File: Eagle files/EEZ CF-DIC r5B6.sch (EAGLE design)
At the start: 260 parts, among them IC1 VIPer35L, IC2 SI8233BB-D-IS1, IC3 LM5041B, IC4 LM258D, IC5 IR11688STRPBF, IC6 LM258D, IC7 TL103W, P1 T910W-50K, Q1 MMBT5551, Q2 C3M0280090D, Q3 C3M0280090D, Q4 NYC0102BLT1G, Q5 C3M0280090D, Q6 C3M0280090D, Q7 FDD86250-F085, Q8 FDD86250-F085, X1 39-30-3035, X2 22-05-7085, X3 B2B-ZR, X4 39-30-1020

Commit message: r5B6 version
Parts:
- added C80: N.C., rcl:C-EUC0805
- added D28: BAS316, EEZ_Lib1:DIODESOD323R
- added L9: IHLP2020CZER3R3M11, EEZ_inductors_and_transformers:IHLP-2020BZ-11
- added Q10, Q9: BC856C, transistor:BC857C-PNP-SOT23-BEC
- added R90: 5K6, rcl:R-EU_R0805
- added R91: 7K5, rcl:R-EU_R0805
- added R92: 220R, rcl:R-EU_R0805
- added R93, R94: 10K, rcl:R-EU_R0805
- added R95: 150K, rcl:R-EU_R0805
- added R96: 39K, rcl:R-EU_R0805
- added R97: 15K, rcl:R-EU_R0805
- added R98: 51K, rcl:R-EU_R0805
- added SH4: (no value), EEZ_Lib1:SHORTNOHOLE
- C1: value MKP-X2-220NR15/310 -> 3n3; device rcl:C-EU150-072X183 -> rcl:C-EUC0805
- C10: value EEEFK1V470P -> 1u; device EEZ_Lib1:ECAPPANASONIC_H -> rcl:C-EUC0805
- C11: value 1u -> EEEFK1V470P; device rcl:C-EUC0805 -> EEZ_Lib1:ECAPPANASONIC_H
- C12: value 1n/1kV -> EEEFK1V470P; device rcl:C-EUC1210 -> EEZ_Lib1:ECAPPANASONIC_H
- C13: value UCY2G6R8MPD -> 1u; device EEZ_Lib1:ECAP5G_10.5MM -> rcl:C-EUC0805
- C14: value EEEFK1V470P -> 1n/1kV; device EEZ_Lib1:ECAPPANASONIC_H -> rcl:C-EUC1210
- C15, C22: value 4u7 -> 3n3; device rcl:C-EUC1206 -> rcl:C-EUC0805
- C16: value 3n3 -> UCY2G6R8MPD; device rcl:C-EUC0805 -> EEZ_Lib1:ECAP5G_10.5MM
- C17: value CY1Y-4N7 -> 3n3; device EEZ_Lib1:C-EUCY -> rcl:C-EUC0805
- C18: value 100n -> EEEFK1V470P; device rcl:C-EUC0603 -> EEZ_Lib1:ECAPPANASONIC_H
- C19: value 3n3 -> 4u7; device rcl:C-EUC0805 -> rcl:C-EUC1206
- C20: value 1500u -> CY1Y-4N7; device EEZ_Lib1:ECAP5G_13MM -> EEZ_Lib1:C-EUCY
- C21: value EEEFK1V470P -> 100n; device EEZ_Lib1:ECAPPANASONIC_H -> rcl:C-EUC0603
- C23: value 33n -> 1500u; device rcl:C-EUC0805 -> EEZ_Lib1:ECAP5G_13MM
- C24: value 100p -> EEEFK1V470P; device rcl:C-EUC0805 -> EEZ_Lib1:ECAPPANASONIC_H
- C25: value 2n2 -> 4u7; device rcl:C-EUC0805 -> rcl:C-EUC1206
- C26: value 1u -> 33n
- C27: value 100n -> 100p; device rcl:C-EUC0603 -> rcl:C-EUC0805
- C28: value 10n -> 2n2; device rcl:C-EUC0603 -> rcl:C-EUC0805
- C29: value 100n -> 1u; device rcl:C-EUC0603 -> rcl:C-EUC0805
- C3: value 3n3 -> MKP-X2-220NR15/310; device rcl:C-EUC0805 -> rcl:C-EU150-072X183
- C31: value UPH2G151MHD6 -> 10n; device EEZ_Lib1:ECAP7.5G_18MM -> rcl:C-EUC0603
- C32: value UPH2G151MHD6 -> 100n; device EEZ_Lib1:ECAP7.5G_18MM -> rcl:C-EUC0603
- C33, C39: value 100n/500V -> 100n; device rcl:C-EUC1812 -> rcl:C-EUC0603
- C34: value 100n -> UPH2G151MHD6; device rcl:C-EUC0603 -> EEZ_Lib1:ECAP7.5G_18MM
- C35: value 10n -> UPH2G151MHD6; device rcl:C-EUC0603 -> EEZ_Lib1:ECAP7.5G_18MM
- C36, C42: value 100n -> 100n/500V; device rcl:C-EUC0603 -> rcl:C-EUC1812
- C38: value 4n7/200V -> 10n; device rcl:C-EUC1210 -> rcl:C-EUC0603
- C4: value CY1Y-4N7 -> N.C.; device EEZ_Lib1:C-EUCY -> rcl:C-EUC0603
- C41: value 1u -> 4n7/200V; device rcl:C-EUC0805 -> rcl:C-EUC1210
- C43: value 1u -> 10n; device rcl:C-EUC0805 -> rcl:C-EUC0603
- C44: value 10n -> 1u; device rcl:C-EUC0603 -> rcl:C-EUC0805
- C46: value 2n2 -> 1u
- C47: value 470p -> 10n; device rcl:C-EUC0805 -> rcl:C-EUC0603
- C48, C71: value 10n -> 100n
- C49: value 100n -> 2n2; device rcl:C-EUC0603 -> rcl:C-EUC0805
- C5: value CY1Y-4N7 -> EEEFK1V470P; device EEZ_Lib1:C-EUCY -> EEZ_Lib1:ECAPPANASONIC_H
- C50: value 1u -> 100p
- C51: value 100n -> 10n
- C52: value N.C. -> 100n
- C54: value UPW1J152MHD -> 100n; device EEZ_Lib1:ECAP7.5G_18MM -> rcl:C-EUC0603
- C55: value UPW1J152MHD -> N.C.; device EEZ_Lib1:ECAP7.5G_18MM -> rcl:C-EUC0603
- C56: value UPW1J152MHD -> 1u; device EEZ_Lib1:ECAP7.5G_18MM -> rcl:C-EUC0805
- C57: value 1u/100V -> UPW1J152MHD; device rcl:C-EUC1206 -> EEZ_Lib1:ECAPH35.5-2A
- C58: value HHXC630ARA330MHA0G -> N.C.; device EEZ_Lib1:ECAPSMD8.3MM/HA0 -> EEZ_Lib1:ECAP7.5G_18MM
- C59: value N.C. -> 1u/100V; device EEZ_Lib1:ECAPSMD8.3MM/HA0 -> rcl:C-EUC1206
- C6: value N.C. -> 1u; device rcl:C-EUC0603 -> rcl:C-EUC0805
- C60: value 1u/100V -> HHXC630ARA330MHA0G; device rcl:C-EUC1206 -> EEZ_Lib1:ECAPSMD8.3MM/HA0
- C61: value 100n/100V -> 1u/100V
- C62: value N.C. -> 100n/100V
- C64: value 100n -> N.C.; device rcl:C-EUC0603 -> rcl:C-EUC1206
- C65: value 4u7 -> 100n; device rcl:C-EUC1206 -> rcl:C-EUC0603
- C66: value 4n7/200V -> 4u7
- C7: value EEEFK1V470P -> CY1Y-4N7; device EEZ_Lib1:ECAPPANASONIC_H -> EEZ_Lib1:C-EUCY
- C70: value 100n -> 4n7/200V; device rcl:C-EUC0603 -> rcl:C-EUC1206
- C72: value 100n -> 1n; device rcl:C-EUC0603 -> rcl:C-EUC0805
- C73, C75: value 100p -> 100n; device rcl:C-EUC0805 -> rcl:C-EUC0603
- C74: value 100n -> 47p; device rcl:C-EUC0603 -> rcl:C-EUC0805
- C76: value 2n2 -> 100p
- C77: value 4u7 -> 470p; device EEZ_Lib1:ECAP1206 -> rcl:C-EUC0805
- C78: value 1u -> 4u7; device rcl:C-EUC0805 -> EEZ_Lib1:ECAP1206
- C79: value N.C. -> 1u
- C8: value 1u -> CY1Y-4N7; device rcl:C-EUC0805 -> EEZ_Lib1:C-EUCY
- D10: value 1N5819HW-7-F -> C3D02065E; device diode:DIODE-SOD323-W -> EEZ_Lib1:SCHOTTKY-SIC
- D11: value C3D06065A -> 1N5819HW-7-F; device EEZ_Lib1:SCHOTTKY-TO220 -> diode:DIODE-SOD323-W
- D12: value 1N5819HW-7-F -> C3D03060A; device diode:DIODE-SOD323-W -> EEZ_Lib1:SCHOTTKY-TO220
- D14: value US1K-DIO -> 1N5819HW-7-F; device EEZ_Lib1:DIODEDO214AA -> diode:DIODE-SOD323-W
- D15: value C3D02065E -> US1K-DIO; device EEZ_Lib1:SCHOTTKY-SIC -> EEZ_Lib1:DIODEDO214AA
- D16: value BAS316 -> C3D02065E; device EEZ_Lib1:DIODESOD323R -> EEZ_Lib1:SCHOTTKY-SIC
- D18, D9: value C3D02065E -> BAS316; device EEZ_Lib1:SCHOTTKY-SIC -> EEZ_Lib1:DIODESOD323R
- D19: value N.C. -> C3D02065E; device diode:DIODE-SOD323-W -> EEZ_Lib1:SCHOTTKY-SIC
- D20, D22: value BAS316 -> N.C.; device EEZ_Lib1:DIODESOD323R -> diode:DIODE-SOD323-W
- D21: value N.C. -> BAS316; device diode:DIODE-SOD323-W -> EEZ_Lib1:DIODESOD323R
- D25: value 1N5819HW-7-F -> BAS316; device diode:DIODE-SOD323-W -> EEZ_Lib1:DIODESOD323R
- D27, D7: value BAS316 -> 1N5819HW-7-F; device EEZ_Lib1:DIODESOD323R -> diode:DIODE-SOD323-W
- D3: value US1K-DIO -> SS110B; device EEZ_Lib1:DIODEDO214AA -> EEZ_Lib1:SCHOTTKYSMB
- D4: value SS110B -> US1K-DIO; device EEZ_Lib1:SCHOTTKYSMB -> EEZ_Lib1:DIODEDO214AA
- D6: value 1N5819HW-7-F -> SS110B; device diode:DIODE-SOD323-W -> EEZ_Lib1:SCHOTTKYSMB
- JP4: value JP3-CUT -> JP2-NOCUT; device EEZ_Lib1:JP3-CUT -> EEZ_Lib1:JP2-NOCUT
- JP5: value JP2-NOCUT -> JP3-CUT; device EEZ_Lib1:JP2-NOCUT -> EEZ_Lib1:JP3-CUT
- L6: value 60B684C -> DLG-0403-180; device EEZ_inductors_and_transformers:MURATA_6000B -> EEZ_inductors_and_transformers:DE0403
- L8: value IHLP2020CZER3R3M11 -> 60B684C; device EEZ_inductors_and_transformers:IHLP-2020BZ-11 -> EEZ_inductors_and_transformers:MURATA_6000B
- Q5, Q6: value C3M0280090D -> IPW60R125P6XKSA1
- R1: value 220K -> 120R; device rcl:R-EU_R1206 -> rcl:R-EU_R0805
- R11: value N.C. -> 120R
- R12: value 47K -> 100K; device rcl:R-EU_R0805 -> rcl:R-EU_R1206
- R13: value 750R -> 100K; device rcl:R-EU_R0805 -> rcl:R-EU_R1206
- R14: value 12K -> 120R
- R15: value 1K8 -> N.C.
- R18: value 10R -> 12K
- R19, R87: value 10K -> 1K8
- R20: value 33R -> 47K
- R21: value 10R -> 1K
- R22: value 100R -> 100K; device rcl:R-EU_R0805 -> rcl:R-EU_R1206
- R23: value 100R -> 10R
- R24: value 22R/2-3W -> 10K; device rcl:R-EU_R2512 -> rcl:R-EU_R0805
- R25: value 22R/2-3W -> 33R; device rcl:R-EU_R2512 -> rcl:R-EU_R0805
- R26: value 1R -> 10R
- R27: value 30K -> 100K; device rcl:R-EU_R0805 -> rcl:R-EU_R1206
- R28: value 33R -> 100R
- R29: value 220K -> 100R; device rcl:R-EU_R1206 -> rcl:R-EU_R0805
- R3, R9: value 120R -> 220K; device rcl:R-EU_R0805 -> rcl:R-EU_R1206
- R30, R40, R69: value 10R -> 22R/2-3W; device rcl:R-EU_R0805 -> rcl:R-EU_R2512
- R31: value 10R -> 100K; device rcl:R-EU_R0805 -> rcl:R-EU_R1206
- R32: value 47K -> 22R/2-3W; device rcl:R-EU_R0805 -> rcl:R-EU_R2512
- R33: value 1R -> 30K
- R34: value 22R/2-3W -> 1R; device rcl:R-EU_R2512 -> rcl:R-EU_R0805
- R35, R53: value 1K -> 33R
- R36, R43: value 100K -> 10R
- R37, R72: value 22R/2-3W -> 10R; device rcl:R-EU_R2512 -> rcl:R-EU_R0805
- R38: value 10R -> 47K
- R39: value 1K -> 1R
- R41: value 10K -> 1K
- R42: value 30K -> 22R/2-3W; device rcl:R-EU_R0805 -> rcl:R-EU_R2512
- R44: value 33R -> 1K
- R45: value 30K -> 10R
- R46: value 82K -> 7K5
- R47: value 33R -> 86K6
- R48: value 1K -> 86K6
- R49: value N.C. -> 33R
- R50: value 6R2 -> 30K
- R52, R86: value 750R -> 86K6
- R54: value 8K2 -> 1K
- R55: value 4K7 -> 6R2
- R56: value 5K6 -> 1K
- R57: value 47K -> 1K
- R58: value 1K -> 4K7
- R59: value 30K -> 5K6
- R6, R7: value 220K -> N.C.; device rcl:R-EU_R1206 -> rcl:R-EU_R0805
- R60: value 10K -> 30K
- R62: value 1K -> 30K
- R63: value 120R -> 10K
- R64: value N.C. -> 1K; device rcl:R-EU_R1210 -> rcl:R-EU_R0805
- R65: value 22R/2-3W -> 1K; device rcl:R-EU_R2512 -> rcl:R-EU_R0805
- R66: value 22R/2-3W -> 120R; device rcl:R-EU_R2512 -> rcl:R-EU_R0805
- R67: value 47K -> N.C.; device rcl:R-EU_R0805 -> rcl:R-EU_R1210
- R68: value 3R3 -> 22R/2-3W; device rcl:R-EU_R0805 -> rcl:R-EU_R2512
- R70: value 47K -> 3R3
- R71: value 3R3 -> 47K
- R73: value 22R/2-3W -> 47K; device rcl:R-EU_R2512 -> rcl:R-EU_R0805
- R74: value 10K -> 3R3
- R75, R76: value 470R -> 22R/2-3W; device rcl:R-EU_R0805 -> rcl:R-EU_R2512
- R77: value 100K -> 10K
- R78: value 10K -> 470R
- R79: value 750R -> 470R
- R8: device rcl:R-EU_R0805 -> rcl:R-EU_R1206
- R80: value 470R -> 150K
- R81: value 51K -> 10K
- R82: value 750R -> 1K
- R85: value 3K3 -> 1K
- R88: value 7K5 -> 3K3
- R89: value 220R -> 1K
- TP6: device EEZ_Lib1:TEST_POINT-2 -> EEZ_connectors:TEST_POINT-2
- TR1: value Feryster 5572 -> FERYSTER_5851; device EEZ_inductors_and_transformers:FERYSTER_5572 -> EEZ_inductors_and_transformers:FERYSTER_5851
- X2: device EEZ_connectors:SPOX_22-05-7085 -> EEZ_connectors:SPOX_22-05-7095
- ZD1: value BZX384-C13 -> BZX384-C15
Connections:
- removed net +15V_REC: C10.+, D2.C, L2.1, R5.1
- removed net -15V: C10.-, C11.2, JP3.COM, TR1.S3, X2-7.1
- removed net 15VAC: C9.2, D2.A, TR1.S3_DOT
- removed net ULVO: D17.A, R36.2, R39.2, R41.1, TP2.2
- new net +12V_REC: C11.+, D2.C, L2.1, R5.1
- new net -12V: C13.2, L4.2, R7.2, X2-3.1
- new net -12V_REC: C12.-, D3.A, L4.1, R10.1
- new net 12VAC1: C9.2, D2.A, TR1.12V_DOT2
- new net 12VAC2: C15.2, D3.C, TR1.12V
- new net 12V_COMM: C10.2, C11.-, C12.+, C13.1, JP3.COM, R6.2, R7.1, TR1.12V_DOT, X2-2.1
- new net ENC_PE: JP2.2
- new net N$60: R12.1, R8.2
- new net N$61: Q10.C, Q9.B, R94.1
- new net N$62: Q10.E, R93.2
- new net N$65: C15.1, R10.2
- new net N$68: R96.2, R97.1, R98.1
- new net N$70: Q10.B, R95.2, R96.1
- new net SYNC_VCC: C65.1, C66.1, IC5.VCC, R72.2
- new net UVLO: C43.1, D18.A, R31.2, R44.2, R46.1, R98.2, TP2.2
- net !FAULT: now also D28.C; no longer D27.C
- net +12V: now also C29.2, C30.2, C52.1, C53.1, R23.2, R36.2, R45.2; no longer C26.2, C27.2, C49.1, C50.1, R18.2, R30.2, R40.2
- net +2.5VREF: now also C79.1, R81.2, R87.1; no longer C78.1, R78.2, R84.1
- net +5VREF: now also C48.2, R43.1, R58.2, R59.2, R93.1, R95.1; no longer C45.2, R38.1, R49.1, R55.2, R56.2
- net +6V_REC: now also C23.+, D6.C, L6.1, R14.1, R17.1; no longer C20.+, D5.C, L5.1, R10.1, R13.1
- net -7V_REC: now also C18.-, D5.A, L5.1, R11.1; no longer C14.-, D4.A, L4.1, R9.1
- net 0V: now also C16.-, C21.1, C24.-, C27.2, C28.2, C29.1, C30.1, C34.-, C35.-, C38.2, C39.2, C4.2, C40.2, C42.1, C44.2, C45.2, C5.-, D12.A, D9.A, JP5.NO, R18.1, R19.2, R20.2, R38.2, R39.1, R39.2, SH2.GND_A, TR1.S_AUX; no longer C13.-, C18.1, C21.-, C24.2, C25.2, C26.1, C27.1, C31.-, C32.-, C33.2, C35.2, C37.2, C39.1, C41.2, C42.2, C7.-, C8.2, D11.A, D8.A, JP4.NO, JP5.2, R14.1, R15.2, R16.2, R32.2, R33.1, R33.2, TR1.S_BIAS
- net 6VAC: now also C22.2, D6.A, TR1.6V_DOT, TR1.7V; no longer C19.2, D5.A, TR1.S1_DOT
- net 7VAC: now also C17.2, D5.C, TR1.7V_DOT; no longer C16.2, D4.C, TR1.S2
- net AC_L_IN: now also C2.2, R3.2; no longer C1.2, R2.2
- net AC_N_IN: now also C2.1, R2.1; no longer C1.1, R1.1
- net AGND: now also C37.1, C43.2, C47.2, C48.1, C49.1, C50.1, C52.2, C54.2, C55.1, C56.1, Q9.C, R33.1, R34.1, R34.2, R50.2, R56.2, R57.2, R63.2, R64.2, R65.2, R94.2, R97.2, SH2.GND_B; no longer C34.1, C40.2, C43.1, C44.2, C45.1, C47.1, C48.2, C49.2, C52.1, C53.1, JP5.1, R26.1, R26.2, R27.1, R41.2, R45.2, R53.2, R54.1, R58.2, R59.2, R60.2
- net AUX_AC: now also C1.2, D8.A, R15.2, TR1.S_AUX_DOT; no longer C3.2, D6.A, R11.2, TR1.S_BIAS_DOT
- net AUX_REC: now also C5.+, R1.1; no longer C7.+, R3.1
- net BUCK_OUT: now also C31.2, C32.2, C33.2, D12.C, L8.P$2; no longer C28.2, C29.2, C30.2, D11.C, L6.P$2
- net CLAMP_C: now also C42.2, D16.C, D19.C, R40.1, R42.1, R48.2; no longer C39.2, D15.C, D18.C, R34.1, R37.1, R43.2
- net COMP: now also C50.2, Q9.E; no longer C47.2, R49.2, R54.2
- net CT_OUT+: now also D21.A, R24.1; no longer D20.A, R19.1
- net CT_OUT-: now also R24.2, R55.2, R57.1; no longer R19.2, R50.2, R53.1
- net DC_BUS: now also C34.+, C35.+, C36.1, D15.C, JP4.1, R22.1; no longer C31.+, C32.+, C33.1, D14.C, JP2.1, R29.1
- net DC_OUT: now also C10.1, R6.1, X2-1.1; no longer C11.1, X2-8.1
- net FB: now also C51.1, R47.1, R56.1, R60.1; no longer C48.1, R42.1, R52.1, R57.1
- net FB2: now also R21.1; no longer R17.1
- net GND: now also C18.+, C19.1, C20.2, C23.-, C25.2, C57.-, C59.2, C60.-, C62.2, C64.1, C66.2, C69.1, C71.2, C73.2, C75.2, C78.-, C80.2, R71.1, R73.2, TR1.6V, X2-4.1, X2-8.1; no longer C14.+, C15.1, C17.2, C20.-, C22.2, C54.-, C55.-, C56.-, C57.2, C59.-, C60.2, C62.1, C64.2, C68.1, C69.2, C72.2, C74.2, C77.-, C78.2, R67.1, R70.2, TR1.S1, TR1.S2_DOT, X2-2.1, X2-6.1
- net HD: now also R28.2; no longer R22.2
- net HI_OUT: now also R25.2, R26.2; no longer R20.2, R21.2
- net LD: now also R29.2; no longer R23.2
- net LO_OUT: now also R35.1, R37.1; no longer R28.1, R31.1
- net L_PULL: now also C41.2, D19.A, L8.P$1; no longer C38.2, D18.A, L7.P$1
- net L_PUSH: now also D16.A, L7.P$1, R30.2; no longer D15.A, L6.P$1, R24.2
- net N$1: now also D28.A, X2-6.1; no longer D27.A, X2-4.1
- net N$10: now also C74.2, R86.1, R90.1; no longer C73.2, R83.1, R87.1
- net N$100: now also C47.1; no longer C44.1
- net N$11: now also R79.2; no longer R76.2
- net N$12: now also R80.1, R84.2; no longer R77.1, R81.2
- net N$126: now also D18.C; no longer D16.C
- net N$13: now also D20.C, R49.1; no longer D19.C, R44.1
- net N$130: now also D17.A, R41.2; no longer D16.A, R35.2
- net N$132: now also R77.2, R81.1; no longer R74.2, R78.1
- net N$133: now also C6.1; no longer C8.1
- net N$134: now also C76.1, R92.2; no longer C75.1, R89.2
- net N$135: now also R17.2; no longer R13.2
- net N$137: now also C14.2, D4.C, R9.2; no longer C12.2, D3.C, R6.2
- net N$138: now also C26.2, C28.1; no longer C23.2, C25.1
- net N$14: now also D22.C, R53.1; no longer D21.C, R47.1
- net N$140: now also C1.1, R1.2; no longer C3.1, R3.2
- net N$141: now also C27.1, R15.1, R16.1, R18.2; no longer C24.1, R11.1, R12.1, R14.2
- net N$144: now also C17.1, R11.2; no longer C16.1, R9.2
- net N$146: now also C22.1, R14.2; no longer C19.1, R10.2
- net N$152: now also C26.1, R20.1; no longer C23.1, R16.1
- net N$155: now also D9.C, R16.2; no longer D7.C, R12.2
- net N$16: now also R78.2; no longer R75.2
- net N$17: now also C41.1, R32.1; no longer C38.1, R25.1
- net N$18: now also R73.1; no longer R70.1
- net N$19: now also R52.1; no longer R46.1
- net N$2: now also R27.2, R31.1; no longer R29.2, R36.1
- net N$20: now also R13.2, R19.1; no longer R15.1, R8.2
- net N$21: now also D11.A, R25.1; no longer D10.A, R20.1
- net N$22: now also R50.1; no longer R45.1
- net N$23: now also C46.2; no longer C43.2
- net N$24: now also C4.1; no longer C6.1
- net N$25: now also R44.1; no longer C40.1, R39.1
- net N$26: now also R58.1, R62.1; no longer R55.1, R59.1
- net N$27: now also C21.2, C24.+, D7.C; no longer C18.2, C21.+, D6.C
- net N$28: now also C72.2, R83.2; no longer C71.2, R80.2
- net N$29: now also D14.A, R35.2, R38.1; no longer D13.A, R28.2, R32.1
- net N$3: now also C31.1, C32.1, C33.1, D10.C; no longer C28.1, C29.1, C30.1, D9.C
- net N$30: now also R47.2, R48.1; no longer R42.2, R43.1
- net N$31: now also D10.A, R23.1; no longer D9.A, R18.1
- net N$32: now also R41.1; no longer R35.1
- net N$33: now also R2.2, R3.1; no longer R1.2, R2.1
- net N$34: now also C56.2, R60.2; no longer C53.2, R57.2
- net N$35: now also D15.A, R40.2, R42.2; no longer D14.A, R34.2, R37.2
- net N$36: now also R28.1; no longer R22.1
- net N$37: now also C49.2, R54.2; no longer C46.2, R48.2
- net N$38: now also D23.A; no longer D22.A
- net N$39: now also C75.1; no longer C74.1
- net N$4: now also C20.1, JP5.COM; no longer C17.1, JP4.COM
- net N$40: now also R29.1; no longer R23.1
- net N$41: now also C3.1, C8.2; no longer C2.1, C5.2
- net N$42: now also C55.2, R63.1; no longer C52.2, R60.1
- net N$43: now also C3.2, C7.2; no longer C2.2, C4.2
- net N$45: now also D11.C, R26.1; no longer D10.C, R21.1
- net N$46: now also C71.1, C73.1, R72.1, R87.2, R88.2; no longer C70.1, C72.1, R69.1, R84.2, R85.2
- net N$47: now also D25.A; no longer D24.A
- net N$48: now also R33.2; no longer R27.2
- net N$49: now also R12.2, R13.1; no longer R7.2, R8.1
- net N$5: now also R30.1, R32.2; no longer R24.1, R25.2
- net N$50: now also R83.1, R84.1, R90.2, R91.2; no longer R80.1, R81.1, R87.2, R88.2
- net N$51: now also D23.C, D25.C, R61.1; no longer D22.C, D24.C, R58.1
- net N$52: now also D14.C, R37.2; no longer D13.C, R31.2
- net N$53: now also R77.1, R82.2; no longer R74.1, R79.2
- net N$54: now also C44.1, C45.1, R45.1; no longer C41.1, C42.1, R40.1
- net N$55: now also C38.1, C39.1, C40.1, D13.C; no longer C35.1, C36.1, C37.1, D12.C
- net N$56: now also D21.C, R54.1, R55.1; no longer D20.C, R48.1, R50.1
- net N$57: now also C80.1; no longer C79.1
- net N$59: now also C53.2, D24.A, R65.1; no longer C50.2, D23.A, R62.1
- net N$6: now also R22.2, R27.1; no longer C64.1, C65.1, IC5.VCC, R69.2
- net N$63: now also D13.A, R36.1; no longer D12.A, R30.1
- net N$64: now also C76.2, R82.1, R85.2, R89.1; no longer C75.2, R79.1, R82.2, R86.1
- net N$66: now also R68.2, R69.2; no longer R65.2, R66.2
- net N$67: now also C70.1, R75.2, R76.2; no longer C69.1, R72.2, R73.2
- net N$7: now also C54.1, D24.C, R59.1, R64.1; no longer C51.1, D23.C, R56.1, R61.1
- net N$74: now also D26.C, R70.2; no longer D25.C, R68.2
- net N$75: now also D27.C, R74.2; no longer D26.C, R71.2
- net N$76: now also C74.1, C77.1; no longer C73.1, C76.1
- net N$8: now also C64.2, R67.1; no longer C62.2, R64.1
- net N$9: now also C77.2, R86.2; no longer C76.2, R83.2
- net NFB_OFFSET: now also C78.+, R85.1, R91.1, R92.1; no longer C77.+, R82.1, R88.1, R89.1
- net OK_A: now also R88.1; no longer R85.1
- net PE: now also C69.2, C7.1, C8.1, JP2.1, JP5.NC; no longer C4.1, C5.1, C66.2, JP4.NC
- net POUT+: now also C57.+, C58.+, C59.1, C67.1, L9.1, R66.1, SH3.GND_B, SH4.GND_A; no longer C54.+, C55.+, C56.+, C57.1, C66.1, L8.1, R63.1, SH2.GND_B, SH3.GND_A
- net PREG_OUT+: now also C60.+, C62.1, C68.1, C72.1, L9.2, R66.2, R71.2, R80.2; no longer C58.+, C59.+, C60.1, C67.1, C71.1, L8.2, R63.2, R64.2, R77.2
- net PULL: now also D22.A, R53.2; no longer D21.A, R47.2
- net PUSH: now also D20.A, R49.2; no longer D19.A, R44.2
- net REF: now also C37.2, R43.2; no longer C34.2, R38.2
- net S1_DOT_OUT: now also R68.1, R69.1; no longer R65.1, R66.1
- net S1_OUT: now also SH3.GND_A; no longer SH2.GND_A
- net S2_DOT_OUT: now also SH4.GND_B; no longer SH3.GND_B
- net S2_OUT: now also R75.1, R76.1; no longer R72.1, R73.1
- net SR_OUT1: now also D26.A, R70.1; no longer D25.A, R68.1
- net SR_OUT2: now also D27.A, R74.1; no longer D26.A, R71.1
- net U_MON1: now also R89.2; no longer R86.2
- net V+: now also C25.1, L6.2, R21.2, R78.1, R79.1, X2-7.1; no longer C22.1, L5.2, R17.2, R75.1, R76.1, X2-3.1
- net V-: now also C19.2, L5.2, X2-9.1; no longer C15.2, L4.2, X2-1.1
- net VIPER+: now also C14.1, C16.+, JP4.2, R8.1, R9.1; no longer C12.1, C13.+, JP2.2, R6.1, R7.1
- net VIPER_D: now also D4.A; no longer D3.A
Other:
- note added: "!FAULT! 6"
- note added: "+12 V"
- note added: "+12V 1"
- note added: "-12 V"
- note added: "-12V 3"
- note added: "12V_GND 2"
- note added: "86K6?"
- note added: "Active Duty cycle limiter"
- note added: "GND 8"
- note added: "IGBT: FGH20N60UFDTU"
- note added: "IGBT: None"
- note added: "IGBT: STGW10M65DF2"
- note added: "NFB with Vout tracker, Duty cycle limiter"
- note added: "U_MON- 4"
- note added: "Use TP2 jumper for testing purposes only when DC_BUS is below 100 Vdc"
- note added: "V(ULVO, max) = 7.8 V => Vin= 374 Vdc (265 Vac) therefore limitation with ZD4 is required"
- note added: "V+ 7"
- note added: "V- 9"
- note added: "X2 9-pin output connector"
- note removed: "!FAULT! 4"
- note removed: "+23 V"
- note removed: "Bias+ 8"
- note removed: "Bias- 7"
- note removed: "NFB with Vout tracker"
- note removed: "U_MON- 6"
- note removed: "Use TP2 jumper for testing purposes only when DC_BUS is below ~85 Vdc"
- note removed: "V(ULVO, max) = 7.8 V => Vin= 374 Vdc (265 Vac) therefore limitation with ZD5 is required"
- note removed: "V+ 3"
- note removed: "V- 1"
- note removed: "X2 8-pin output connector"
- moved on the sheet: C1, C15, C17, C19, C2, C22, C25, C29, C3, C30, C33, C36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

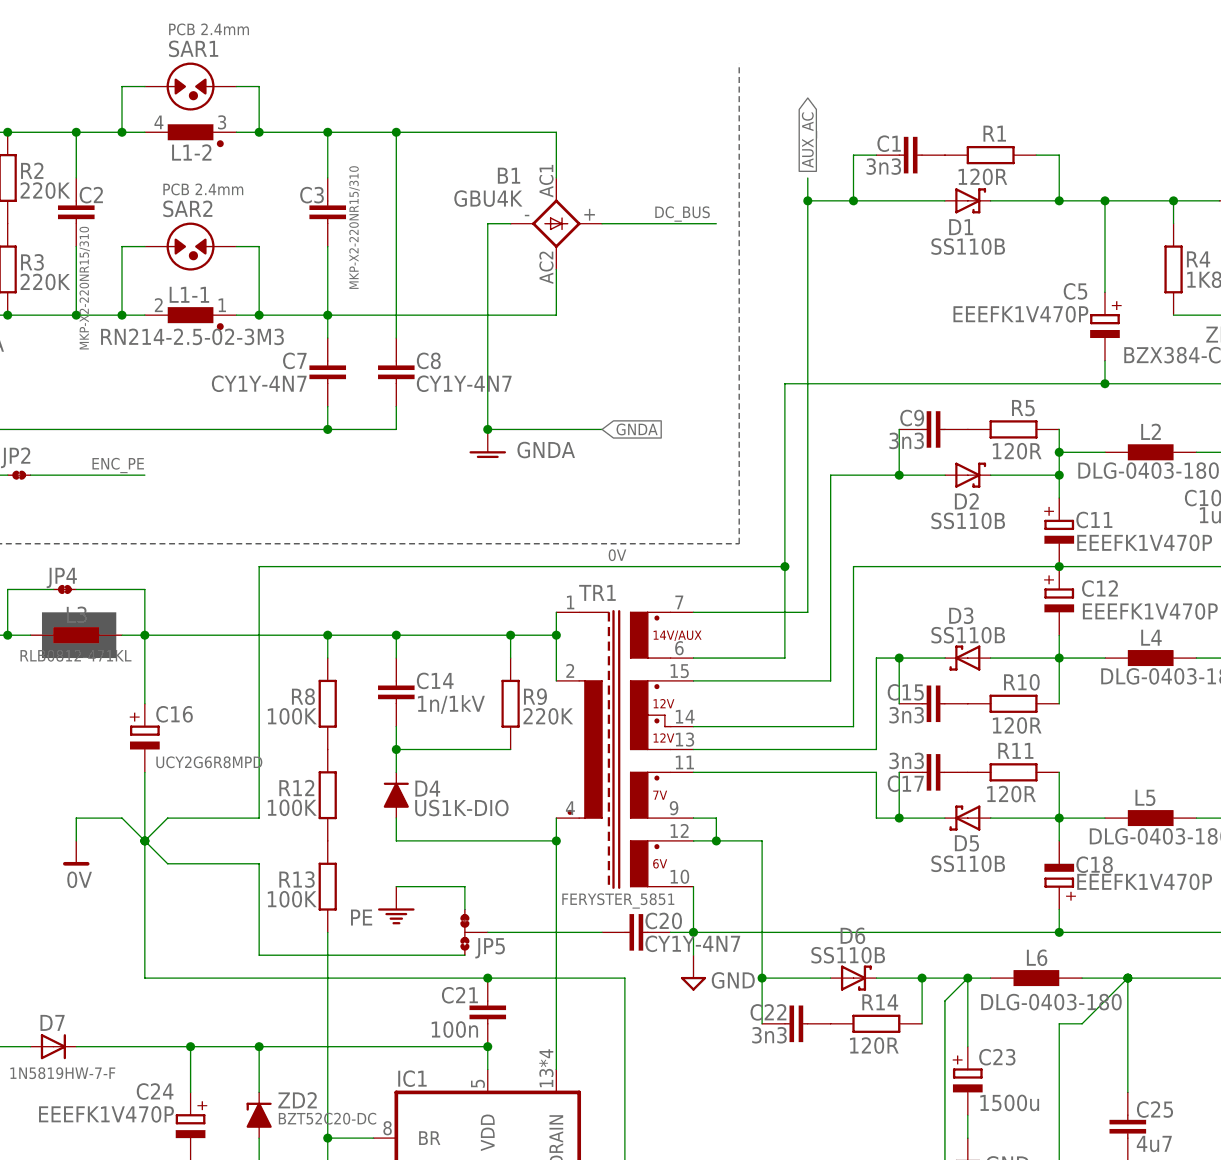
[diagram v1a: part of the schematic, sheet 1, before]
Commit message: 7V secondary wiring fix
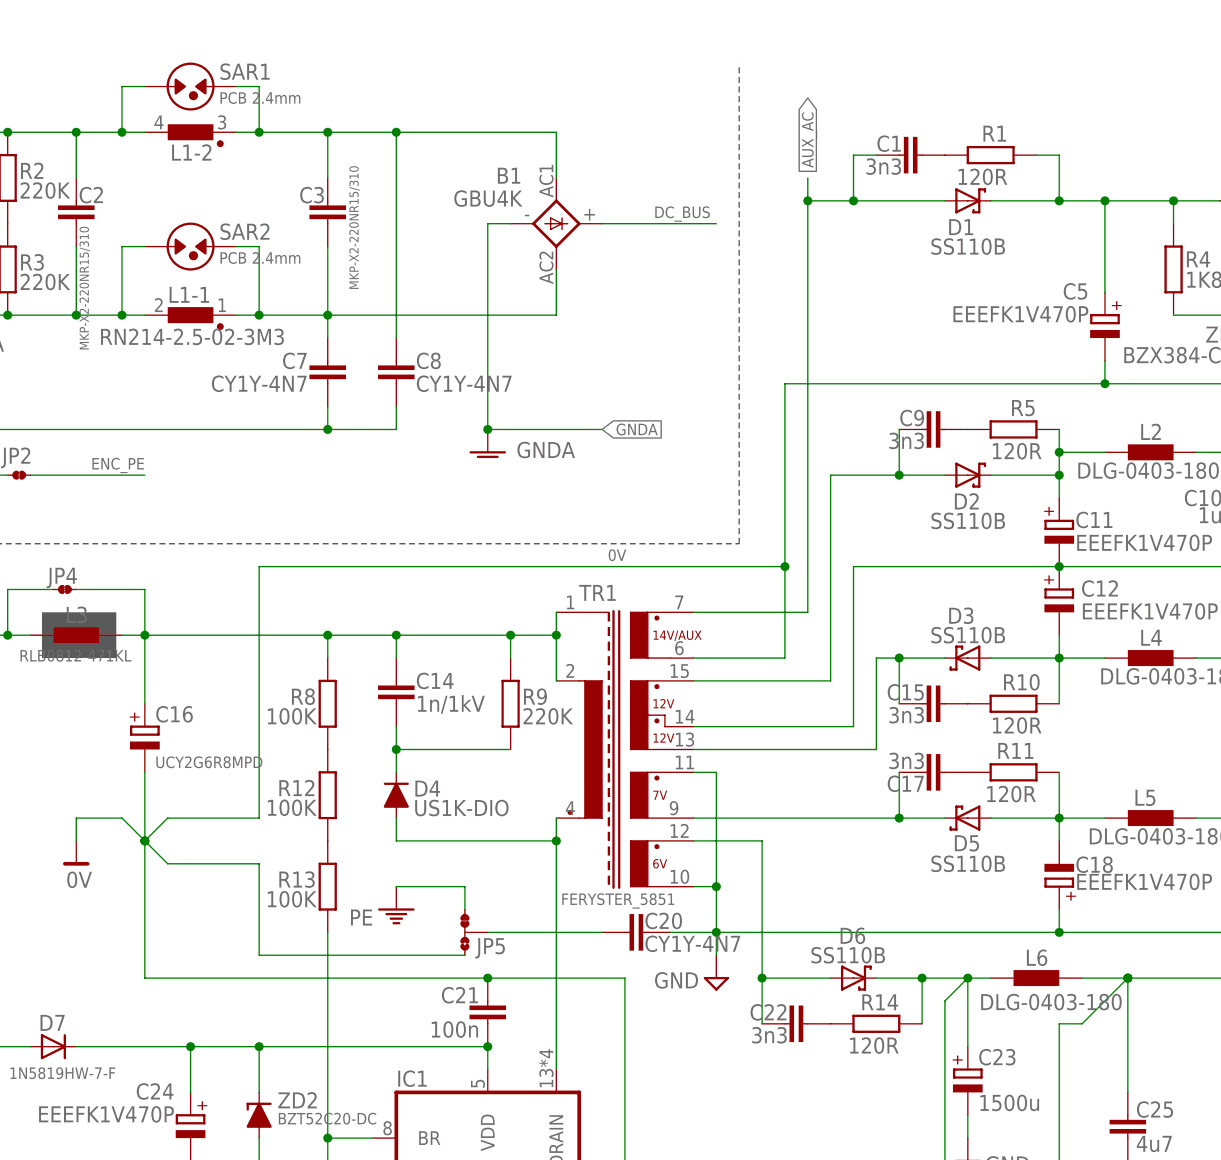
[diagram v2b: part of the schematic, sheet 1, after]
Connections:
- net 6VAC: no longer TR1.7V
- net 7VAC: now also TR1.7V; no longer TR1.7V_DOT
- net GND: now also TR1.7V_DOT
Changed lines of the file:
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@@
 <attribute name="VALUE" x="37.465" y="42.418" size="1.778" layer="96" rot="MR0"/>
 </instance>
-<instance part="SUPPLY22" gate="GND" x="106.68" y="73.66" smashed="yes">
-<attribute name="VALUE" x="108.585" y="74.295" size="1.778" layer="96" rot="MR180"/>
+<instance part="SUPPLY22" gate="GND" x="109.22" y="73.66" smashed="yes">
+<attribute name="VALUE" x="107.315" y="74.295" size="1.778" layer="96" rot="R180"/>
 </instance>
 <instance part="R9" gate="G$1" x="86.36" y="104.14" smashed="yes" rot="R270">
@@
 </instance>
 <instance part="SAR2" gate="G$1" x="50.8" y="154.94" smashed="yes" rot="MR270">
-<attribute name="NAME" x="47.625" y="160.02" size="1.778" layer="95" rot="MR180"/>
-<attribute name="VALUE" x="47.625" y="161.925" size="1.27" layer="96" rot="MR180"/>
+<attribute name="NAME" x="53.975" y="157.48" size="1.778" layer="95" rot="MR180"/>
+<attribute name="VALUE" x="53.975" y="154.305" size="1.27" layer="96" rot="MR180"/>
 </instance>
 <instance part="B1" gate="G$1" x="91.44" y="157.48" smashed="yes">
@@
 </instance>
 <instance part="SAR1" gate="G$1" x="50.8" y="172.72" smashed="yes" rot="MR270">
-<attribute name="NAME" x="48.26" y="177.8" size="1.778" layer="95" rot="MR180"/>
-<attribute name="VALUE" x="48.26" y="179.705" size="1.27" layer="96" rot="MR180"/>
+<attribute name="NAME" x="53.975" y="175.26" size="1.778" layer="95" rot="MR180"/>
+<attribute name="VALUE" x="53.975" y="172.085" size="1.27" layer="96" rot="MR180"/>
 </instance>
 <instance part="SUPPLY10" gate="1" x="205.74" y="96.52" smashed="yes" rot="MR270">
@@
 <segment>
 <pinref part="D5" gate="G$1" pin="C"/>
-<wire x1="127" y1="91.44" x2="129.54" y2="91.44" width="0.1524" layer="91"/>
 <pinref part="C17" gate="G$1" pin="2"/>
-<pinref part="TR1" gate="G$1" pin="7V_DOT"/>
 <wire x1="129.54" y1="91.44" x2="134.62" y2="91.44" width="0.1524" layer="91"/>
-<wire x1="106.68" y1="96.52" x2="127" y2="96.52" width="0.1524" layer="91"/>
-<wire x1="127" y1="96.52" x2="127" y2="91.44" width="0.1524" layer="91"/>
 <wire x1="129.54" y1="96.52" x2="129.54" y2="91.44" width="0.1524" layer="91"/>
 <junction x="129.54" y="91.44"/>
+<pinref part="TR1" gate="G$1" pin="7V"/>
+<wire x1="106.68" y1="91.44" x2="129.54" y2="91.44" width="0.1524" layer="91"/>
 </segment>
 </net>
@@
 <segment>
 <pinref part="C20" gate="G$1" pin="2"/>
-<wire x1="104.14" y1="78.74" x2="106.68" y2="78.74" width="0.1524" layer="91"/>
 <pinref part="SUPPLY22" gate="GND" pin="GND"/>
-<wire x1="106.68" y1="83.82" x2="106.68" y2="78.74" width="0.1524" layer="91"/>
 <pinref part="TR1" gate="G$1" pin="6V"/>
-<wire x1="106.68" y1="76.2" x2="106.68" y2="78.74" width="0.1524" layer="91"/>
-<junction x="106.68" y="78.74"/>
 <wire x1="170.18" y1="78.74" x2="147.32" y2="78.74" width="0.1524" layer="91"/>
 <pinref part="C18" gate="G$1" pin="+"/>
@@
 <pinref part="C19" gate="G$1" pin="1"/>
 <wire x1="170.18" y1="81.28" x2="170.18" y2="78.74" width="0.1524" layer="91"/>
-<wire x1="106.68" y1="78.74" x2="147.32" y2="78.74" width="0.1524" layer="91"/>
+<wire x1="104.14" y1="78.74" x2="109.22" y2="78.74" width="0.1524" layer="91"/>
 <junction x="147.32" y="78.74"/>
+<pinref part="TR1" gate="G$1" pin="7V_DOT"/>
+<wire x1="109.22" y1="78.74" x2="147.32" y2="78.74" width="0.1524" layer="91"/>
+<wire x1="106.68" y1="96.52" x2="109.22" y2="96.52" width="0.1524" layer="91"/>
+<wire x1="109.22" y1="96.52" x2="109.22" y2="83.82" width="0.1524" layer="91"/>
+<wire x1="109.22" y1="83.82" x2="106.68" y2="83.82" width="0.1524" layer="91"/>
+<wire x1="109.22" y1="83.82" x2="109.22" y2="78.74" width="0.1524" layer="91"/>
+<junction x="109.22" y="83.82"/>
+<junction x="109.22" y="78.74"/>
+<wire x1="109.22" y1="78.74" x2="109.22" y2="76.2" width="0.1524" layer="91"/>
 </segment>
 <segment>
@@
 <junction x="114.3" y="73.66"/>
 <pinref part="TR1" gate="G$1" pin="6V_DOT"/>
-<wire x1="106.68" y1="88.9" x2="109.22" y2="88.9" width="0.1524" layer="91"/>
-<pinref part="TR1" gate="G$1" pin="7V"/>
-<wire x1="109.22" y1="88.9" x2="114.3" y2="88.9" width="0.1524" layer="91"/>
-<wire x1="106.68" y1="91.44" x2="109.22" y2="91.44" width="0.1524" layer="91"/>
-<wire x1="109.22" y1="91.44" x2="109.22" y2="88.9" width="0.1524" layer="91"/>
-<junction x="109.22" y="88.9"/>
-</segment>
-</net>
+<wire x1="106.68" y1="88.9" x2="114.3" y2="88.9" width="0.1524" layer="91"/>
+</segment>
+</net>
